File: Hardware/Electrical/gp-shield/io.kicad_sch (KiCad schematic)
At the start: 0 parts

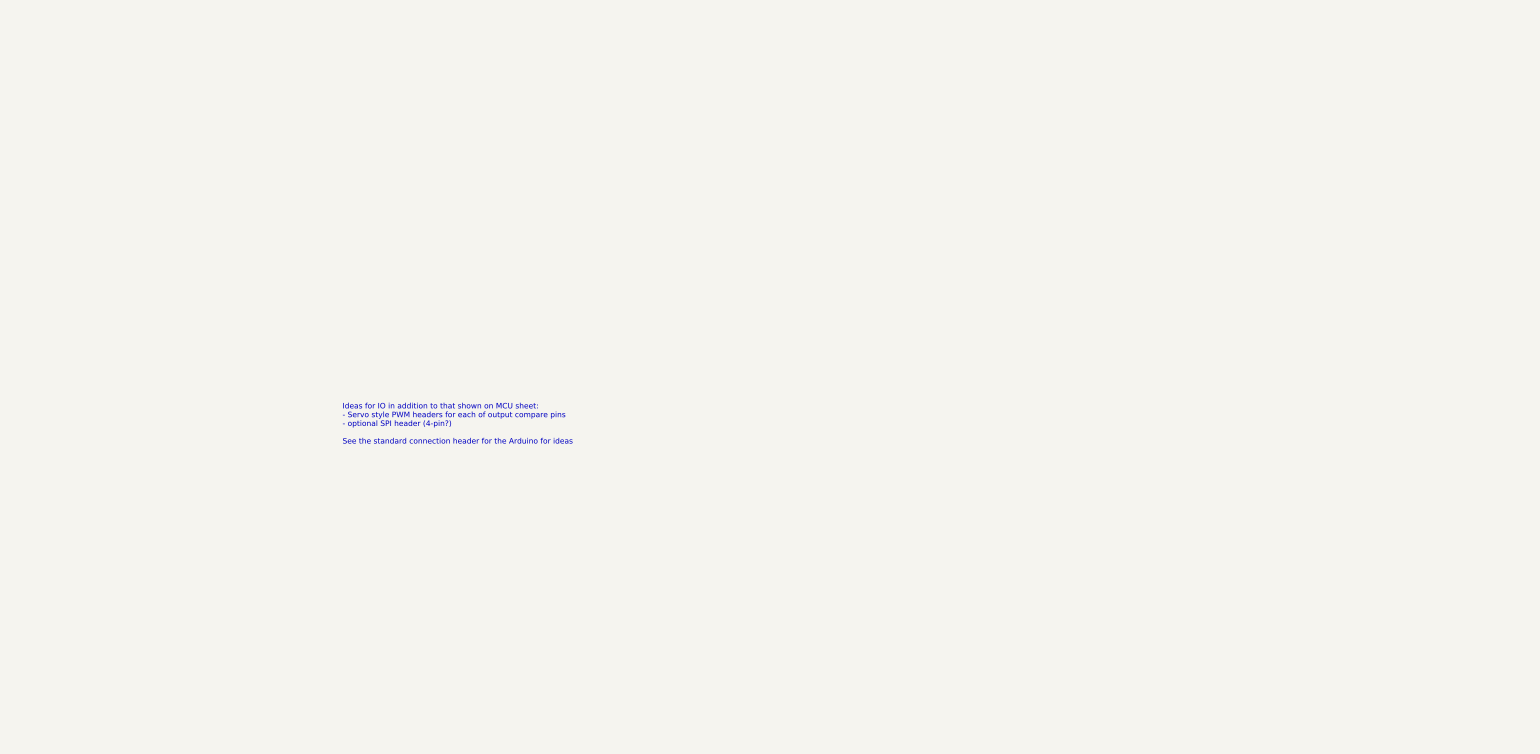
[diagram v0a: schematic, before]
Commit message: Major revisions to PCB layout
- near final layout
- prototype version of silkscreen
- removed 3.3V reg
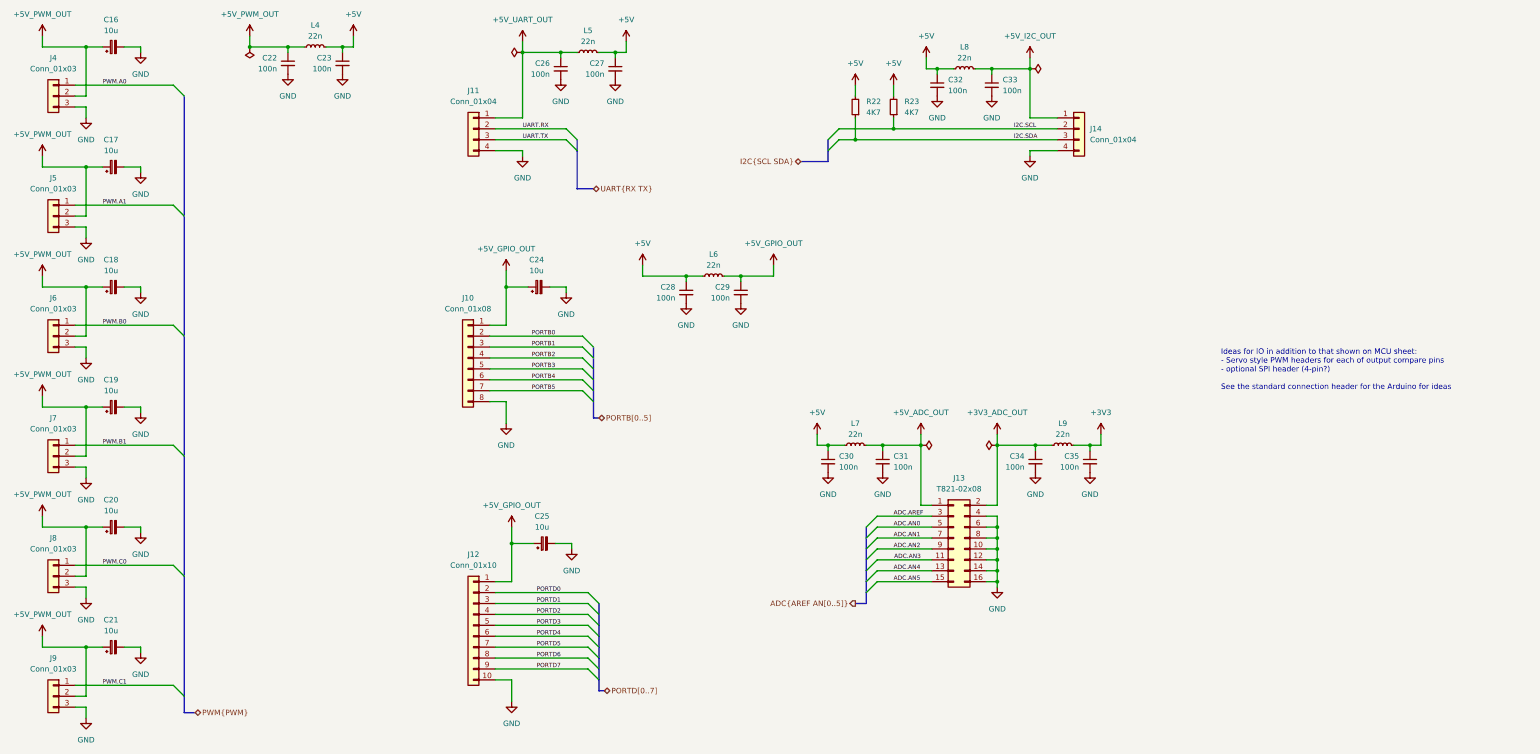
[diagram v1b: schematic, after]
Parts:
- added C16, C17, C18, C19, C20, C21, C24, C25: 10u, Capacitor_SMD:C_0805_2012Metric_Pad1.18x1.45mm_HandSolder, symbol Device:C_Polarized_Small
- added C22, C23, C26, C27, C28, C29, C30, C31, C32, C33, C34, C35: 100n, Capacitor_SMD:C_0805_2012Metric_Pad1.18x1.45mm_HandSolder, symbol Device:C_Small
- added J10: Conn_01x08, Connector_PinSocket_2.54mm:PinSocket_1x08_P2.54mm_Vertical, symbol Connector_Generic:Conn_01x08
- added J11, J14: Conn_01x04, Connector_Molex:Molex_KK-254_AE-6410-04A_1x04_P2.54mm_Vertical, symbol Connector_Generic:Conn_01x04
- added J12: Conn_01x10, Connector_PinSocket_2.54mm:PinSocket_1x10_P2.54mm_Vertical, symbol Connector_Generic:Conn_01x10
- added J13: T821-02x08, Connector_IDC:IDC-Header_2x08_P2.54mm_Horizontal, symbol Connector_Generic:Conn_02x08_Odd_Even
- added J4, J5, J6, J7, J8, J9: Conn_01x03, Connector_PinHeader_2.54mm:PinHeader_1x03_P2.54mm_Vertical, symbol Connector_Generic:Conn_01x03
- added L4, L5, L6, L7, L8, L9: 22n, Inductor_SMD:L_0805_2012Metric_Pad1.15x1.40mm_HandSolder, symbol Device:L_Small
- added R22, R23: 4K7, Resistor_SMD:R_0805_2012Metric_Pad1.20x1.40mm_HandSolder, symbol Device:R_Small
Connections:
- new net +3V3: C35.1, L9.1
- new net +3V3_ADC_OUT: C34.1, J13.2 (Pin_2), L9.2
- new net +5V: C23.1, C27.1, C28.1, C30.1, C32.1, L4.1, L5.1, L6.2, L7.1, L8.1, R22.2, R23.2
- new net +5V_ADC_OUT: C24.1, C25.1, C31.1, J10.1 (Pin_1), J12.1 (Pin_1), J13.1 (Pin_1), L7.2
- new net +5V_GPIO_OUT: C29.1, L6.1
- new net +5V_I2C_OUT: C33.1, J14.1 (Pin_1), L8.2
- new net +5V_PWM_OUT: C16.1, C17.1, C18.1, C19.1, C20.1, C21.1, C22.1, J4.2 (Pin_2), J5.2 (Pin_2), J6.2 (Pin_2), J7.2 (Pin_2), J8.2 (Pin_2), J9.2 (Pin_2), L4.2
- new net +5V_UART_OUT: C26.1, J11.1 (Pin_1), L5.2
- new net ADC.AN0: J13.5 (Pin_5)
- new net ADC.AN1: J13.7 (Pin_7)
- new net ADC.AN2: J13.9 (Pin_9)
- new net ADC.AN3: J13.11 (Pin_11)
- new net ADC.AN4: J13.13 (Pin_13)
- new net ADC.AN5: J13.15 (Pin_15)
- new net ADC.AREF: J13.3 (Pin_3)
- new net GND: C16.2, C17.2, C18.2, C19.2, C20.2, C21.2, C22.2, C23.2, C24.2, C25.2, C26.2, C27.2, C28.2, C29.2, C30.2, C31.2, C32.2, C33.2, C34.2, C35.2, J10.8 (Pin_8), J11.4 (Pin_4), J12.10 (Pin_10), J13.10 (Pin_10), J13.12 (Pin_12), J13.14 (Pin_14), J13.16 (Pin_16), J13.4 (Pin_4), J13.6 (Pin_6), J13.8 (Pin_8), J14.4 (Pin_4), J4.3 (Pin_3), J5.3 (Pin_3), J6.3 (Pin_3), J7.3 (Pin_3), J8.3 (Pin_3), J9.3 (Pin_3)
- new net I2C.SCL: J14.2 (Pin_2), R23.1
- new net I2C.SDA: J14.3 (Pin_3), R22.1
- new net PORTB0: J10.2 (Pin_2)
- new net PORTB1: J10.3 (Pin_3)
- new net PORTB2: J10.4 (Pin_4)
- new net PORTB3: J10.5 (Pin_5)
- new net PORTB4: J10.6 (Pin_6)
- new net PORTB5: J10.7 (Pin_7)
- new net PORTD0: J12.2 (Pin_2)
- new net PORTD1: J12.3 (Pin_3)
- new net PORTD2: J12.4 (Pin_4)
- new net PORTD3: J12.5 (Pin_5)
- new net PORTD4: J12.6 (Pin_6)
- new net PORTD5: J12.7 (Pin_7)
- new net PORTD6: J12.8 (Pin_8)
- new net PORTD7: J12.9 (Pin_9)
- new net PWM.A0: J4.1 (Pin_1)
- new net PWM.A1: J5.1 (Pin_1)
- new net PWM.B0: J6.1 (Pin_1)
- new net PWM.B1: J7.1 (Pin_1)
- new net PWM.C0: J8.1 (Pin_1)
- new net PWM.C1: J9.1 (Pin_1)
- new net UART.RX: J11.2 (Pin_2)
- new net UART.TX: J11.3 (Pin_3)

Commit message: Major revisions
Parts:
- renumbered C16 to C11, C17 to C12, C18 to C13, C19 to C14, C20 to C15, C21 to C16, C22 to C17, C23 to C18, C24 to C19, C25 to C20, C26 to C21, C27 to C22, C28 to C23, C29 to C24, C30 to C25, C31 to C26, C32 to C27, C33 to C28, C34 to C29, C35 to C30, L4 to L3, L5 to L4, L6 to L5, L7 to L6, L8 to L7, L9 to L8, R22 to R19, R23 to R20

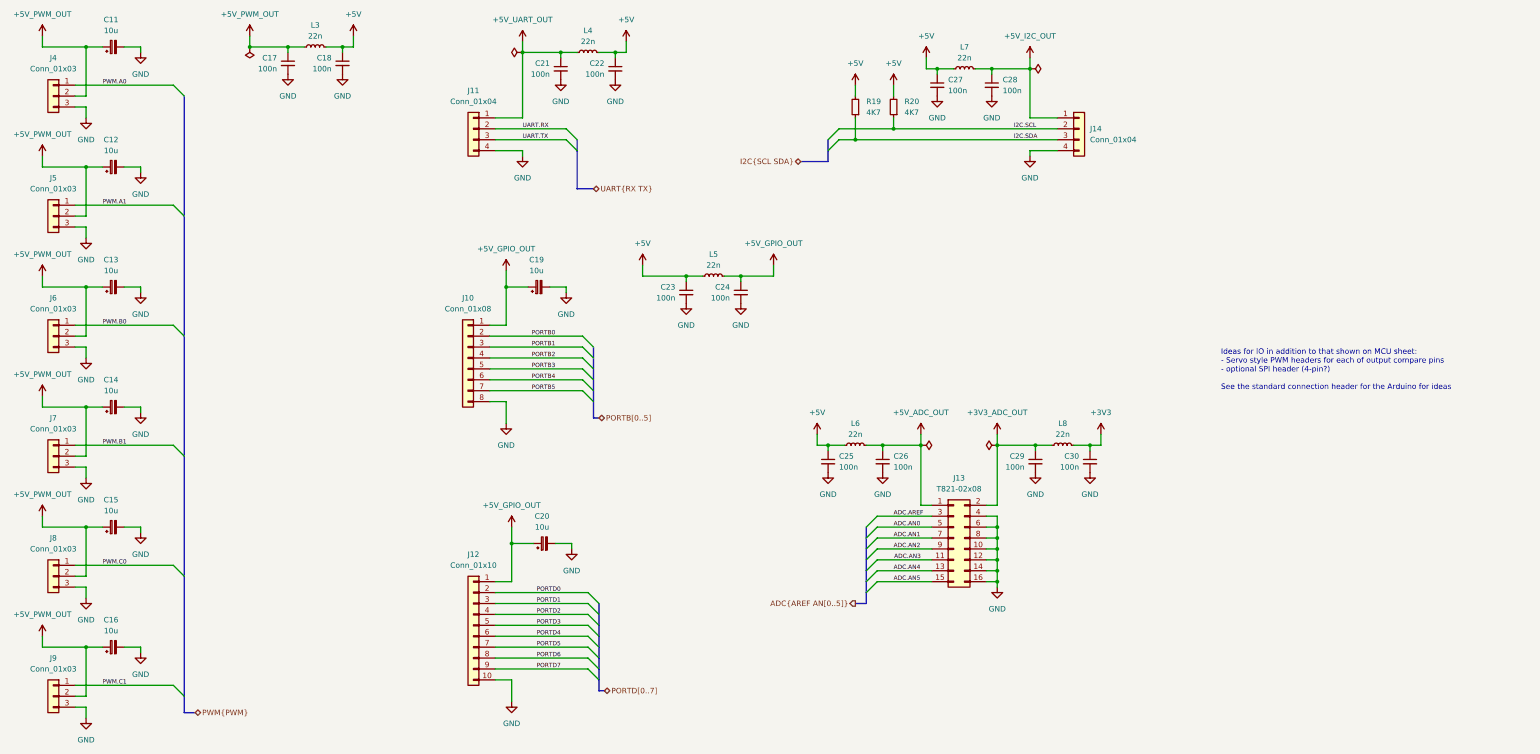
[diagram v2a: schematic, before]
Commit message: Major PCB changes
Added combined footprint for XT60 and terminal port.
Fixed polarity of Batt and PWR_out connectors.
Standardised polarity markers to show negative on white.
Moved Port D and Port B connectors to be inline with existing arduino connectors. Removed extra pins.
Added analogue in-line output.
Adjusted component placement for more space around power supply and GP PB and LED.
Draft version of track routing - incomplete.
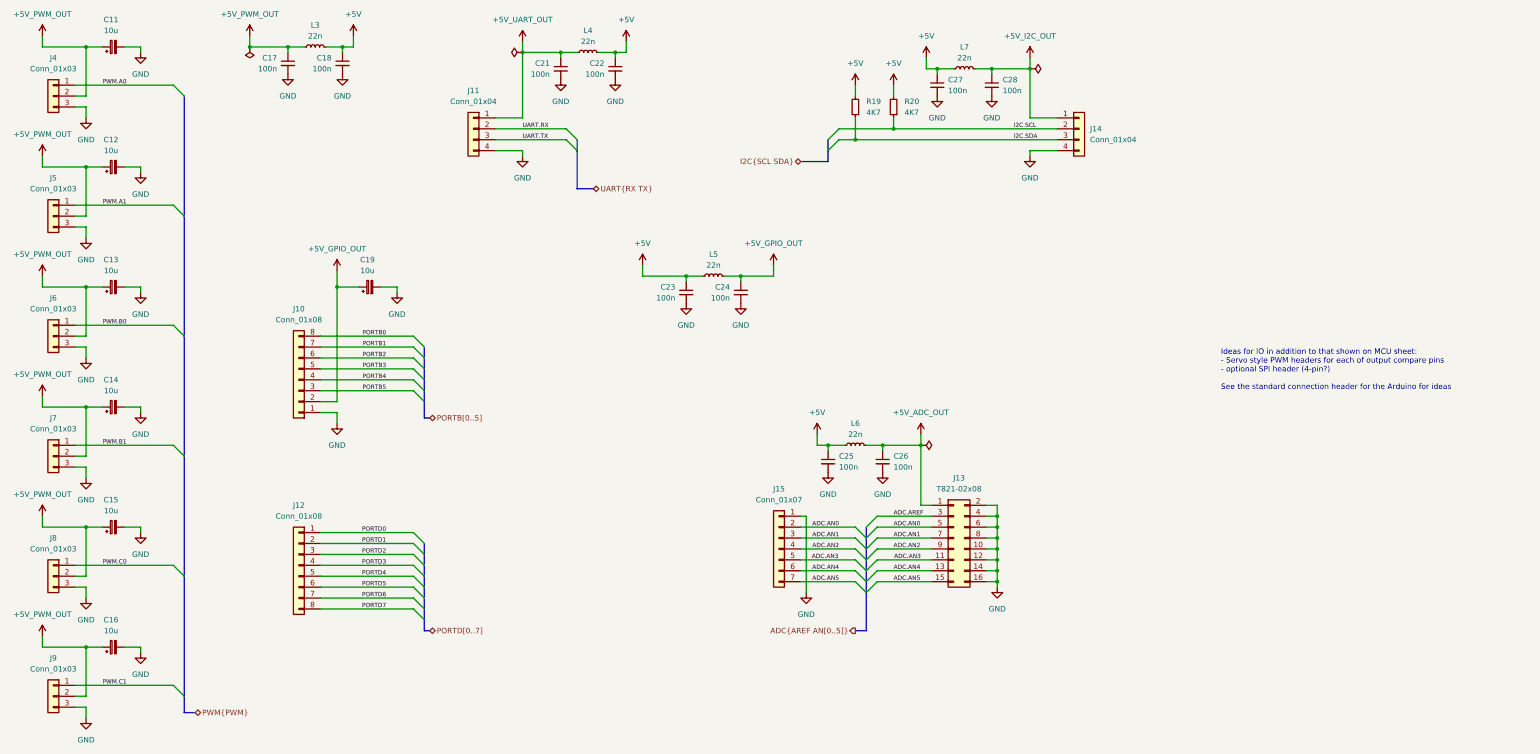
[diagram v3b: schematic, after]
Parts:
- removed C20: 10u, Capacitor_SMD:C_0805_2012Metric_Pad1.18x1.45mm_HandSolder, symbol Device:C_Polarized_Small
- removed C29, C30: 100n, Capacitor_SMD:C_0805_2012Metric_Pad1.18x1.45mm_HandSolder, symbol Device:C_Small
- removed J12: Conn_01x10, Connector_PinSocket_2.54mm:PinSocket_1x10_P2.54mm_Vertical, symbol Connector_Generic:Conn_01x10
- removed L8: 22n, Inductor_SMD:L_0805_2012Metric_Pad1.15x1.40mm_HandSolder, symbol Device:L_Small
- added J12: Conn_01x08, Connector_PinSocket_2.54mm:PinSocket_1x08_P2.54mm_Vertical, symbol Connector_Generic:Conn_01x08
- added J15: Conn_01x07, Connector_PinSocket_2.54mm:PinSocket_1x07_P2.54mm_Vertical, symbol Connector_Generic:Conn_01x07
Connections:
- net +3V3_ADC_OUT is gone; now on net GND: J13.2 (Pin_2)
- net +5V_ADC_OUT: now also J10.2 (Pin_2); no longer J10.1 (Pin_1)
- net ADC.AN0: now also J15.2 (Pin_2)
- net ADC.AN1: now also J15.3 (Pin_3)
- net ADC.AN2: now also J15.4 (Pin_4)
- net ADC.AN3: now also J15.5 (Pin_5)
- net ADC.AN4: now also J15.6 (Pin_6)
- net ADC.AN5: now also J15.7 (Pin_7)
- net GND: now also J10.1 (Pin_1), J15.1 (Pin_1); no longer J10.8 (Pin_8)
- net PORTB0: now also J10.8 (Pin_8); no longer J10.2 (Pin_2)
- net PORTB1: now also J10.7 (Pin_7); no longer J10.3 (Pin_3)
- net PORTB2: now also J10.6 (Pin_6); no longer J10.4 (Pin_4)
- net PORTB4: now also J10.4 (Pin_4); no longer J10.6 (Pin_6)
- net PORTB5: now also J10.3 (Pin_3); no longer J10.7 (Pin_7)
- net PORTD0: now also J12.1 (Pin_1)
- net PORTD1: now also J12.2 (Pin_2)
- net PORTD2: now also J12.3 (Pin_3)
- net PORTD3: now also J12.4 (Pin_4)
- net PORTD4: now also J12.5 (Pin_5)
- net PORTD5: now also J12.6 (Pin_6)
- net PORTD6: now also J12.7 (Pin_7)
- net PORTD7: now also J12.8 (Pin_8)
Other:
- moved on the sheet: C19

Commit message: Complete draft PCB layout
Added updated renders to doc.
Added some documentation to schematic
complete PCB layout with some revisions still needed
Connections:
- net +5V_ADC_OUT: no longer C19.1, J10.2 (Pin_2)
- net +5V_GPIO_OUT: now also C19.1, J10.2 (Pin_2)
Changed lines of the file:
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@@
     (pin "2")
-  )
-  (symbol (lib_id "Utility:+5V_GPIO_OUT") (at 92.71 77.47 0) (unit 1)
-    (in_bom yes) (on_board yes) (fields_autoplaced)
-    (property "Reference" "#PWR096" (id 0) (at 92.71 81.28 0)
-      (effects (font (size 1.27 1.27)) hide)
-    )
-    (property "Value" "+5V_GPIO_OUT" (id 1) (at 92.71 72.39 0))
-    (property "Footprint" "" (id 2) (at 92.71 77.47 0)
-      (effects (font (size 1.27 1.27)) hide)
-    )
-    (property "Datasheet" "" (id 3) (at 92.71 77.47 0)
-      (effects (font (size 1.27 1.27)) hide)
-    )
-    (pin "1")
   )
   (symbol (lib_id "power:GND") (at 232.41 36.83 0) (unit 1)
@@
     (pin "4")
   )
-  (symbol (lib_name "+5V_GPIO_OUT_1") (lib_id "Utility:+5V_GPIO_OUT") (at 194.31 76.2 0) (unit 1)
-    (in_bom yes) (on_board yes) (fields_autoplaced)
-    (property "Reference" "#PWR0110" (id 0) (at 194.31 80.01 0)
-      (effects (font (size 1.27 1.27)) hide)
-    )
-    (property "Value" "+5V_GPIO_OUT" (id 1) (at 194.31 71.12 0))
-    (property "Footprint" "" (id 2) (at 194.31 76.2 0)
-      (effects (font (size 1.27 1.27)) hide)
-    )
-    (property "Datasheet" "" (id 3) (at 194.31 76.2 0)
-      (effects (font (size 1.27 1.27)) hide)
-    )
-    (pin "1")
-  )
   (symbol (lib_id "power:+5V") (at 222.25 34.29 0) (unit 1)
     (in_bom yes) (on_board yes) (fields_autoplaced)
@@
     (pin "1")
   )
+  (symbol (lib_id "Utility:+5V_GPIO_OUT") (at 194.31 76.2 0) (unit 1)
+    (in_bom yes) (on_board yes) (fields_autoplaced)
+    (property "Reference" "#PWR0120" (id 0) (at 194.31 80.01 0)
+      (effects (font (size 1.27 1.27)) hide)
+    )
+    (property "Value" "+5V_GPIO_OUT" (id 1) (at 194.31 71.12 0))
+    (property "Footprint" "" (id 2) (at 194.31 76.2 0)
+      (effects (font (size 1.27 1.27)) hide)
+    )
+    (property "Datasheet" "" (id 3) (at 194.31 76.2 0)
+      (effects (font (size 1.27 1.27)) hide)
+    )
+    (pin "1")
+  )
   (symbol (lib_id "Utility:+5V_PWM_OUT") (at 24.13 22.86 0) (unit 1)
     (in_bom yes) (on_board yes) (fields_autoplaced)
@@
       (effects (font (size 1.27 1.27)) hide)
     )
+    (pin "1")
+  )
+  (symbol (lib_id "Utility:+5V_GPIO_OUT") (at 92.71 77.47 0) (unit 1)
+    (in_bom yes) (on_board yes) (fields_autoplaced)
+    (property "Reference" "#PWR0110" (id 0) (at 92.71 81.28 0)
+      (effects (font (size 1.27 1.27)) hide)
+    )
+    (property "Value" "+5V_GPIO_OUT" (id 1) (at 92.71 72.39 0))
+    (property "Footprint" "" (id 2) (at 92.71 77.47 0)
+      (effects (font (size 1.27 1.27)) hide)
+    )
+    (property "Datasheet" "" (id 3) (at 92.71 77.47 0)
+      (effects (font (size 1.27 1.27)) hide)
+    )

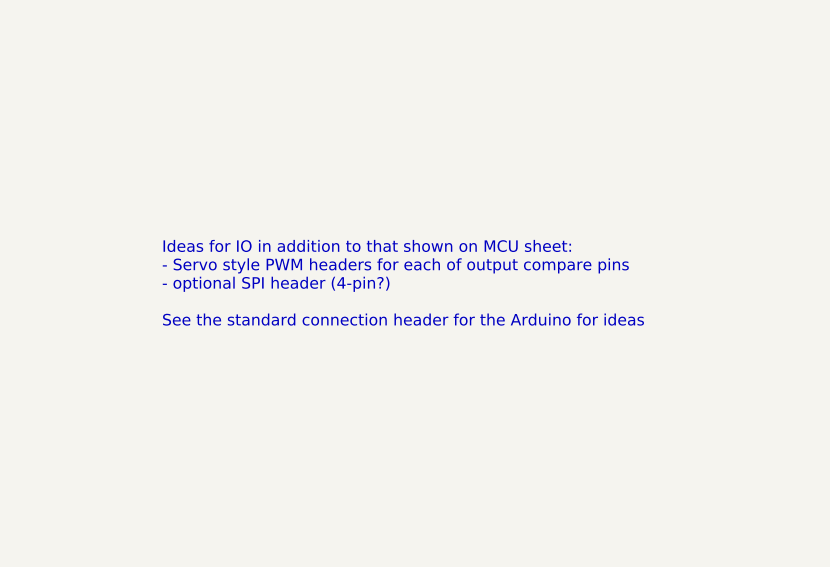
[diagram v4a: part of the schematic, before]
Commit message: Minor cosmetic imporvements
title block and colour theme
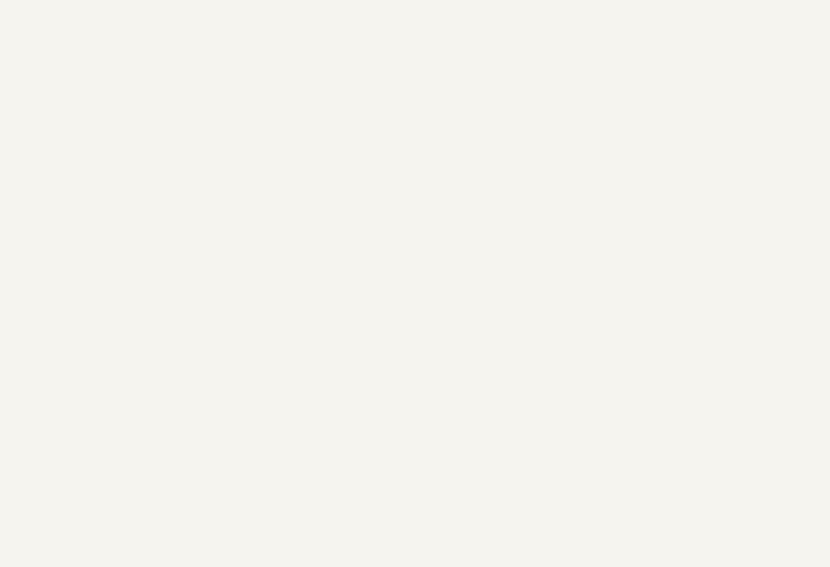
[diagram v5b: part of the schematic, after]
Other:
- note removed: "Ideas for IO in addition to that shown on MCU sheet: - Servo style PWM headers for each of output compare pins - optional SPI header (4-pin?) See the standard connection header for the Arduino for ideas"
- company: (none) -> University of Tasmania
- title: (none) -> gp-shield IO
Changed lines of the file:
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@@
 (kicad_sch (version 20211123) (generator eeschema)
   (paper "A4")
+  (title_block
+    (title "gp-shield IO")
+    (date "2022-12-01")
+    (rev "1")
+    (company "University of Tasmania")
+  )
   (bus_alias "PWM" (members "A[0..1]" "B[0..2]" "C[0..2]"))
   (junction (at 213.36 46.99) (diameter 0) (color 0 0 0 0)
@@
     (stroke (width 0) (type default) (color 0 0 0 0))
   )
-  (text "Ideas for IO in addition to that shown on MCU sheet:\n- Servo style PWM headers for each of output compare pins\n- optional SPI header (4-pin?)\n\nSee the standard connection header for the Arduino for ideas"
-    (at 298.45 105.41 0)
-    (effects (font (size 1.27 1.27)) (justify left bottom))
-  )
   (label "ADC.AN5" (at 209.55 149.86 180)
